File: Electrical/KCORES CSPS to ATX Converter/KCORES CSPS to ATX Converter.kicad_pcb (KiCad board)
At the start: 2 copper layers, 86.1 x 86.1 mm, 26 parts, among them J1 CSPS, J2 PMBUS, J3 GW_PCIe/CPU, J4 GW_PCIe/CPU, J5 GW_PCIe/CPU, J6 GW_PCIe/CPU, J7 GW_PCIe/CPU, J8 IDE/SATA, J9 GW_24P_ATX, U1 Mini560 5V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

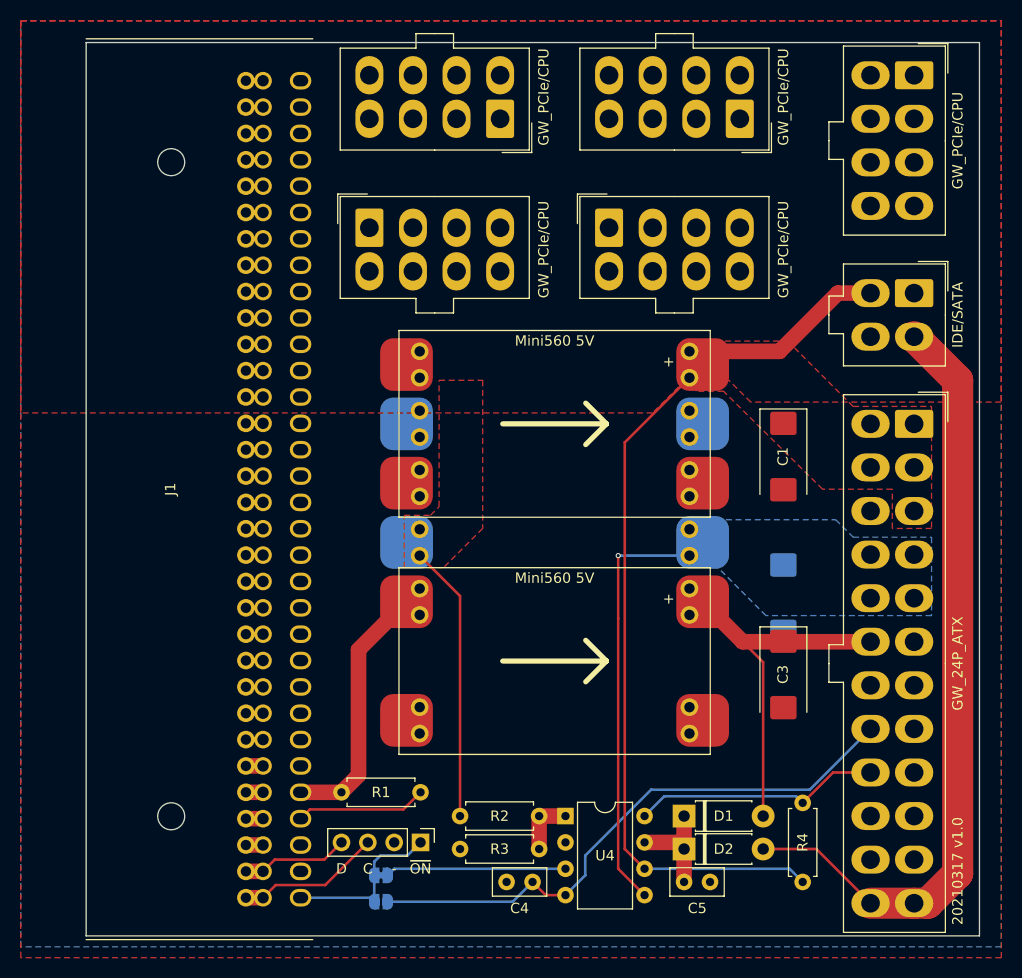
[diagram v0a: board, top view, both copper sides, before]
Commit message: Change modules
Used PW22 DC to DC modules instead of defaults
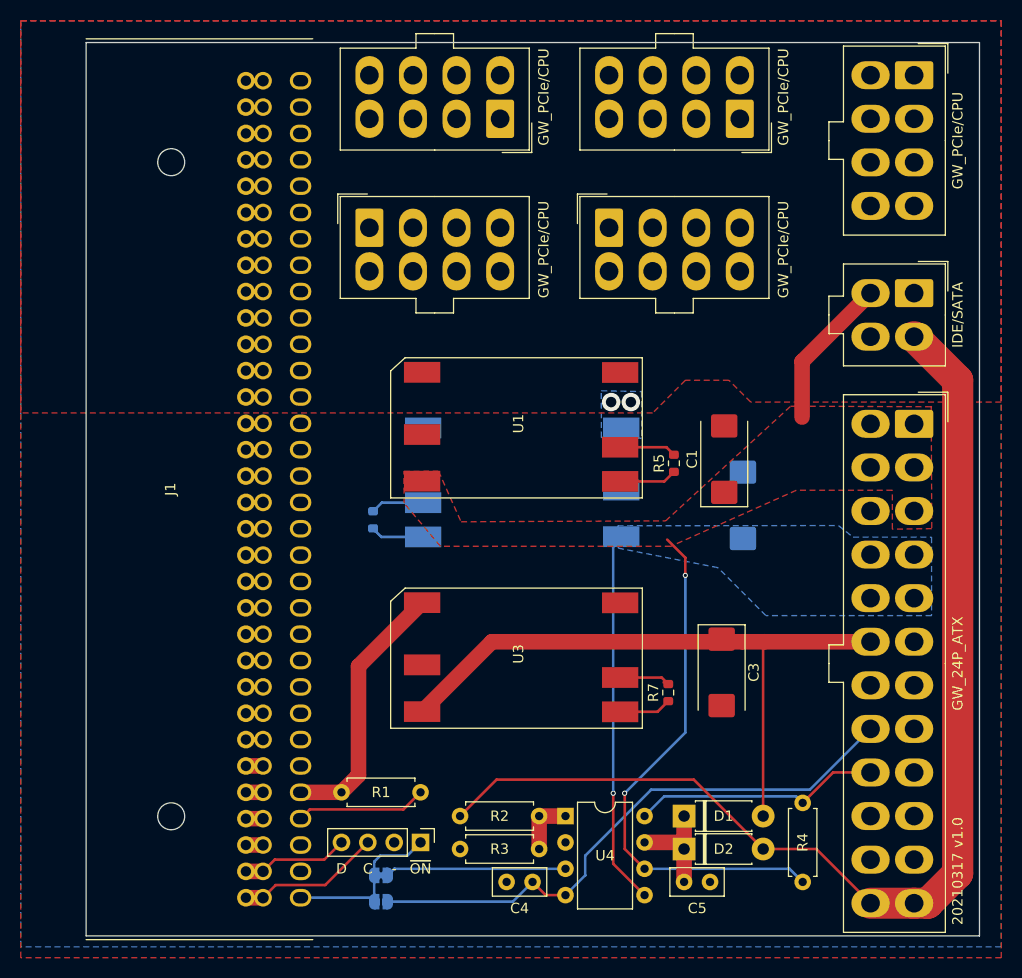
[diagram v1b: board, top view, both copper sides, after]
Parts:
- added R5: R, Resistor_SMD:R_0603_1608Metric, F.Cu at (149.1, 117.2)
- added R6: R, Resistor_SMD:R_0603_1608Metric, B.Cu at (120.0, 122.7)
- added R7: R, Resistor_SMD:R_0603_1608Metric, F.Cu at (148.5, 139.3)
- U1, U3: value Mini560 5V -> PW22 5V; footprint KCORES_Converter_DCDC:Converter_DCDC_Mini_560 -> KCORES_Converter_DCDC:PW22
- U2: value Mini560 3.3V -> PW22 3.3V; footprint KCORES_Converter_DCDC:Converter_DCDC_Mini_560 -> KCORES_Converter_DCDC:PW22
- moved U2 19.9 mm to (123.0, 132.7), turned to 90 degrees
- moved U1 16.2 mm to (145.8, 127.3), turned to 90 degrees
- moved U3 15.6 mm to (145.8, 149.6), turned to 90 degrees
- moved C2 9.76 mm to (155.7, 121.2), turned to 90 degrees
- moved C3 5.95 mm to (153.7, 137.3)
- moved C1 5.71 mm to (153.9, 116.8), turned to 90 degrees
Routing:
- net /+5VSB: track 35.4 -> 62.8 mm
- net +5V: track 86.2 -> 66.1 mm, vias 0 -> 2
- net +12V: track 102.3 -> 109.0 mm, vias 0 -> 2
- net Net-(R5-Pad1): track 0.00 -> 5.56 mm
- net Net-(R5-Pad2): track 0.00 -> 5.48 mm
- net Net-(R7-Pad2): track 0.00 -> 5.39 mm
- net +3V3: track 41.5 -> 36.1 mm
- net Net-(R6-Pad2): track 0.00 -> 5.18 mm
- net Net-(R6-Pad1): track 0.00 -> 5.16 mm
- net Net-(R7-Pad1): track 0.00 -> 5.05 mm
- net /+12VSB: track 24.9 -> 25.4 mm
- added copper zone on B.Cu, net +12V

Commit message: Used SMD Packages
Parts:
- C4, C5: footprint Capacitor_THT:C_Disc_D5.0mm_W2.5mm_P2.50mm -> Capacitor_SMD:C_0603_1608Metric
- R1, R2, R3, R4: footprint Resistor_THT:R_Axial_DIN0207_L6.3mm_D2.5mm_P7.62mm_Horizontal -> Resistor_SMD:R_0603_1608Metric
- U4: footprint Package_DIP:DIP-8_W7.62mm -> KCORES_Converter_DCDC:SOIC127P599X175-8N
- moved R4 21.8 mm to (139.7, 149.5), turned to 0 degrees
- moved C5 17.2 mm to (134.8, 149.5), turned to 180 degrees
- moved R3 9.13 mm to (129.8, 145.3)
- moved U4 6.83 mm to (132.3, 153.9)
- moved R2 5.98 mm to (134.8, 145.3), turned to 0 degrees
- moved R1 5.26 mm to (129.8, 149.6), turned to 0 degrees
- moved C4 2.51 mm to (130.7, 158.6), turned to 180 degrees
- moved D2 0.12 mm to (150.0, 154.5)
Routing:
- net +5V: track 66.1 -> 49.6 mm
- net Net-(C5-Pad1): track 10.4 -> 24.2 mm, vias 0 -> 3
- net /ATX_PWOK: track 24.0 -> 37.2 mm, vias 0 -> 2
- net /+12VSB: track 25.4 -> 38.4 mm
- net /~ATX_PSON: track 55.6 -> 67.5 mm, vias 0 -> 2
- net +12V: track 109.0 -> 101.5 mm
- net /~FPO: track 17.4 -> 10.5 mm, vias 0 -> 1
- net Net-(R2-Pad1): track 5.72 -> 11.0 mm
- net /~PRESENT: track 12.6 -> 16.7 mm
- net +3V3: track 36.1 -> 37.4 mm
